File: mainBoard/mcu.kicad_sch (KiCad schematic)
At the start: 20 parts, among them Q1 IRLML6244TRPBF, SW2 SW_SPDT, U4 STM32F401RETx, Y2 ATS08A-E

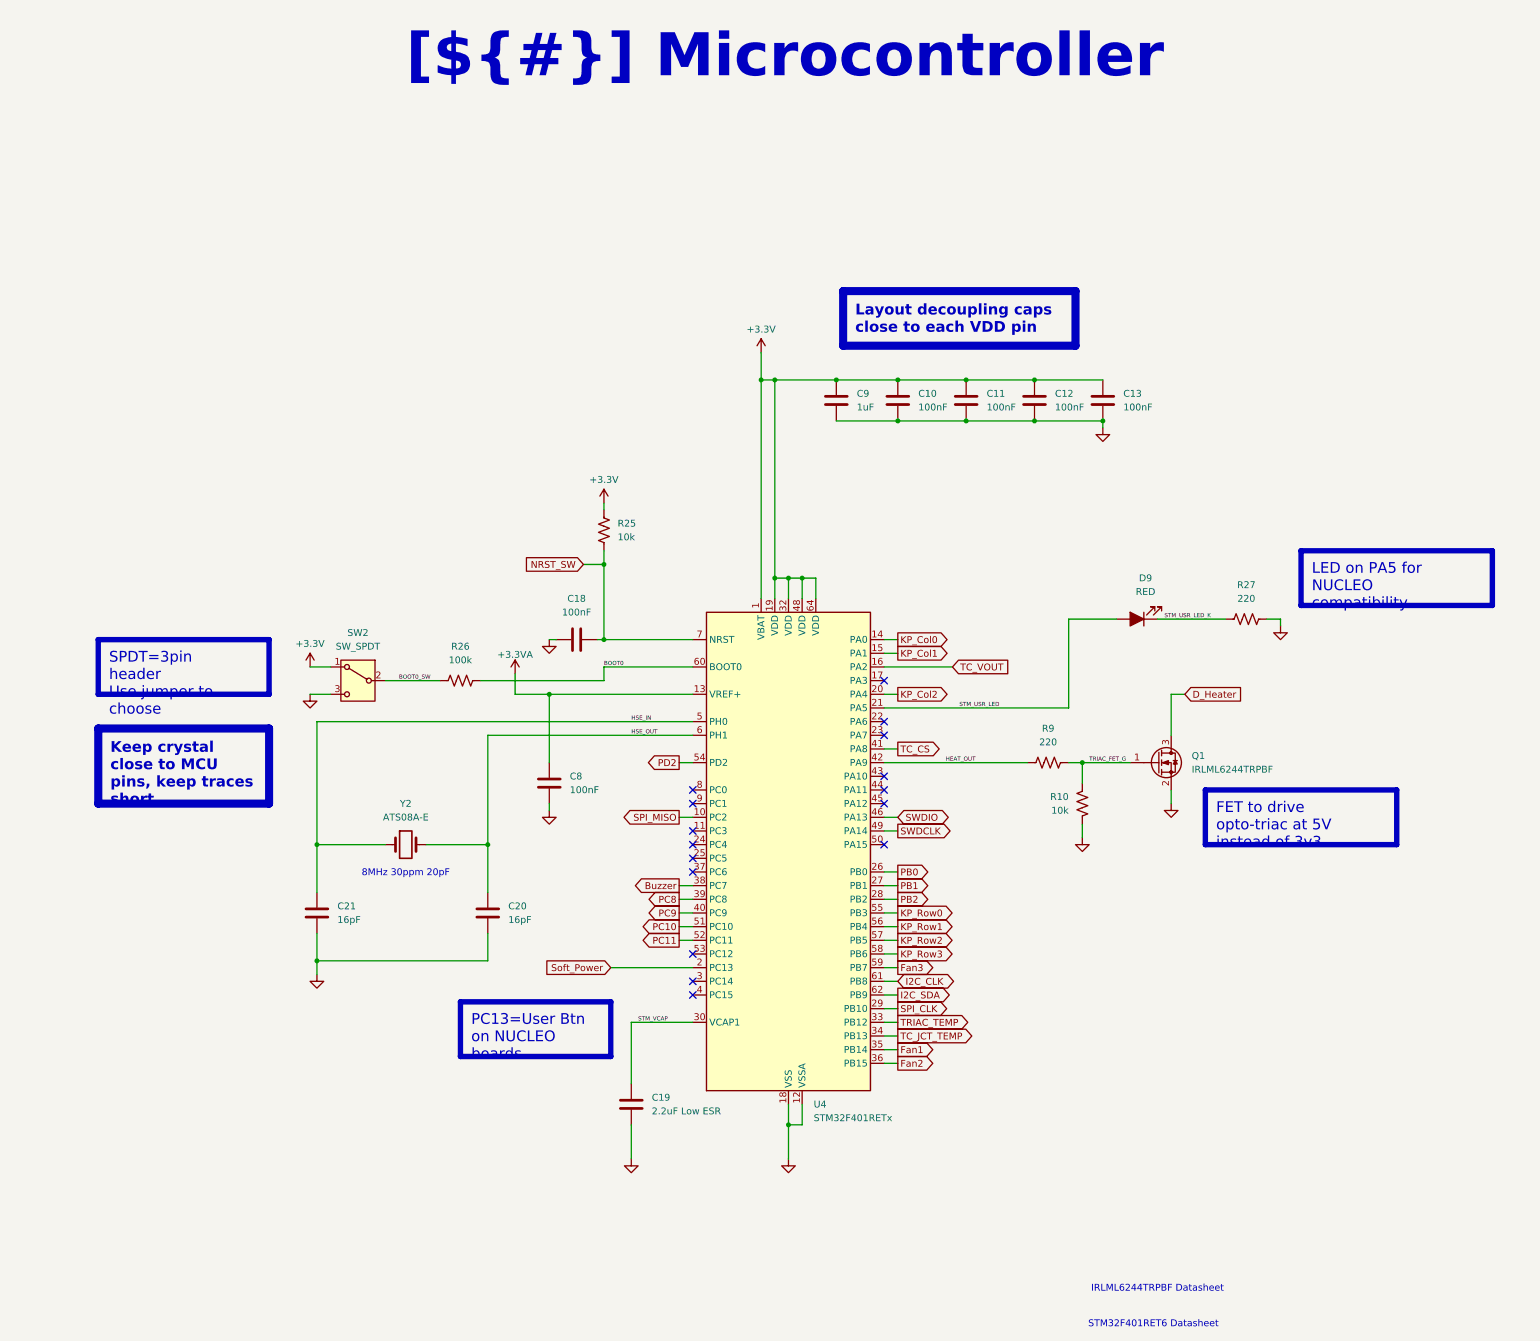
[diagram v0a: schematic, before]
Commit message: Add net colors and tweak MCU
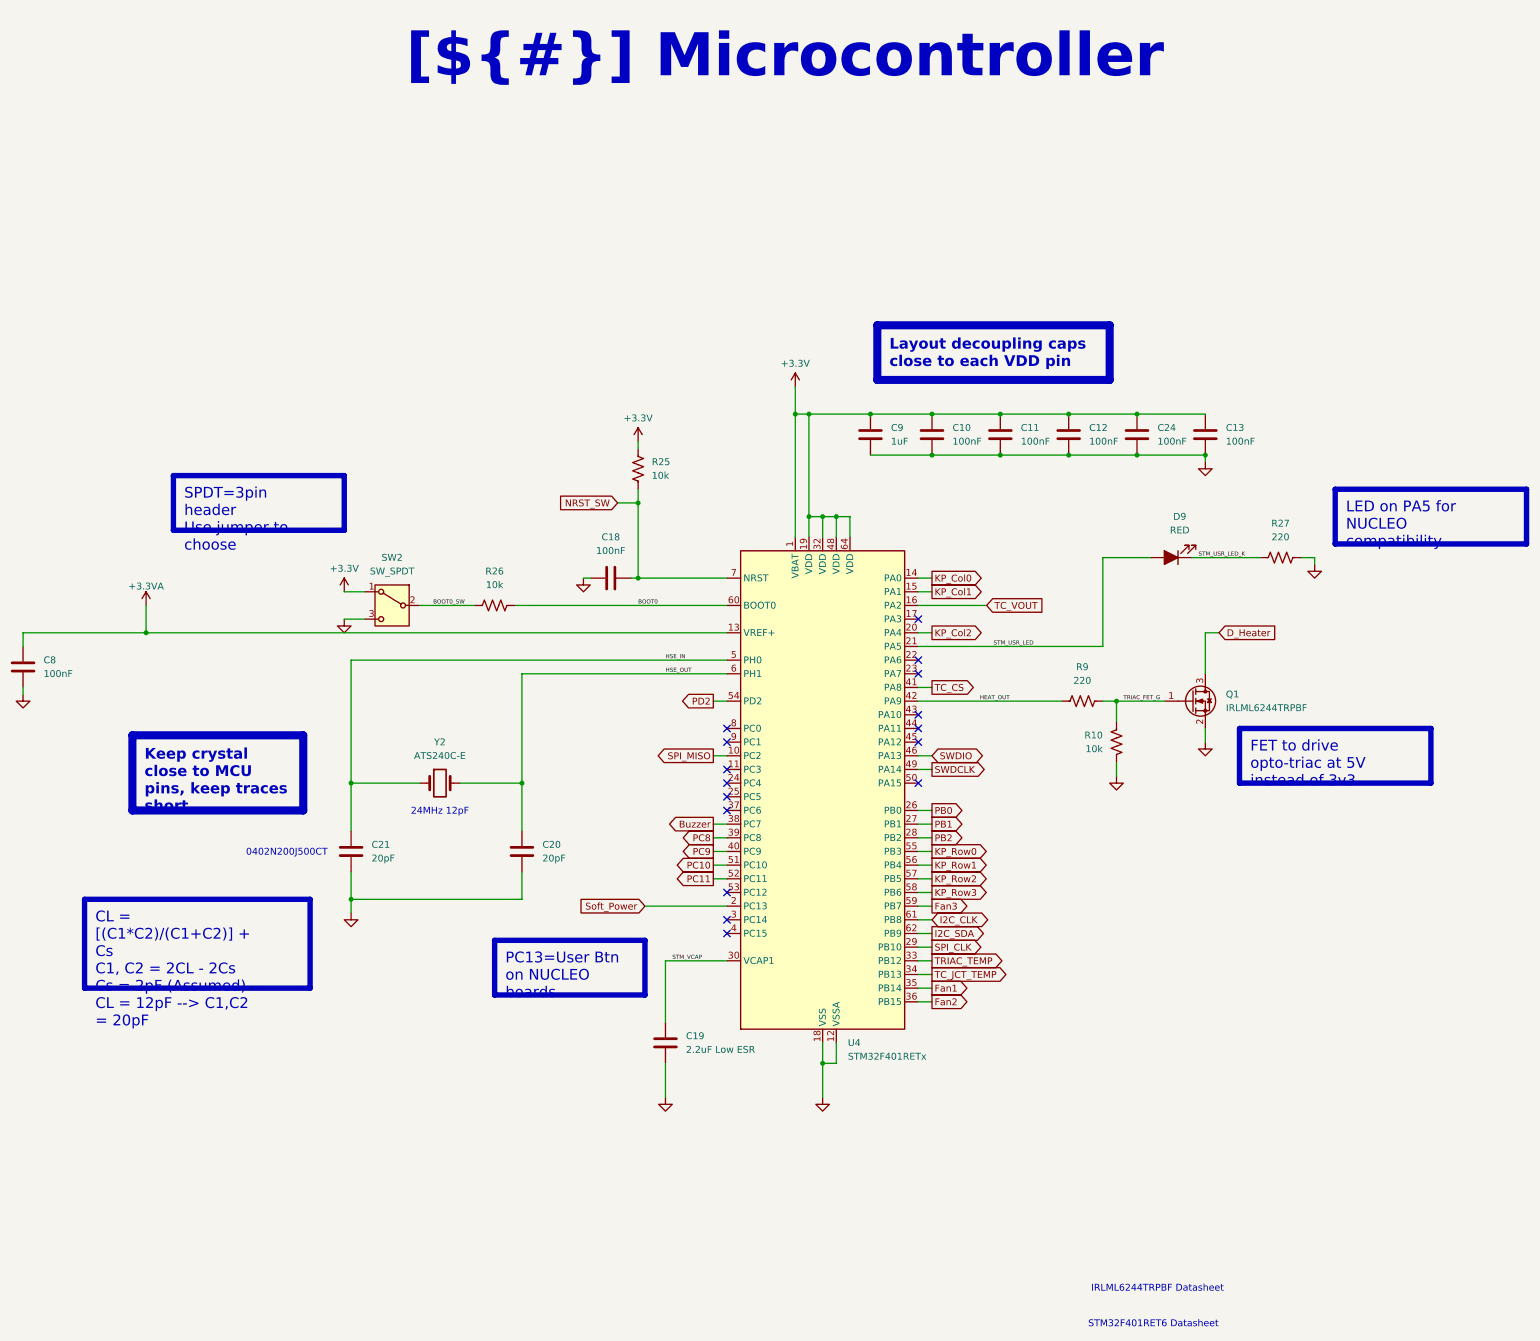
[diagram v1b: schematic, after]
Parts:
- added C24: 100nF, Capacitor_SMD:C_0603_1608Metric_Pad1.08x0.95mm_HandSolder, symbol Device:C
- C20, C21: value 16pF -> 20pF
- R26: value 100k -> 10k
- Y2: value ATS08A-E -> ATS240C-E
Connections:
- net +3.3V: now also C24.1
- net GND: now also C24.2
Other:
- note added: "0402N200J500CT"
- note added: "24MHz 12pF"
- note removed: "8MHz 30ppm 20pF"
- moved on the sheet: C10, C11, C12, C13, C18, C19, C20, C21, C8, C9, D9, Q1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

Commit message: Schematic Capture should be complete, ready for PCB
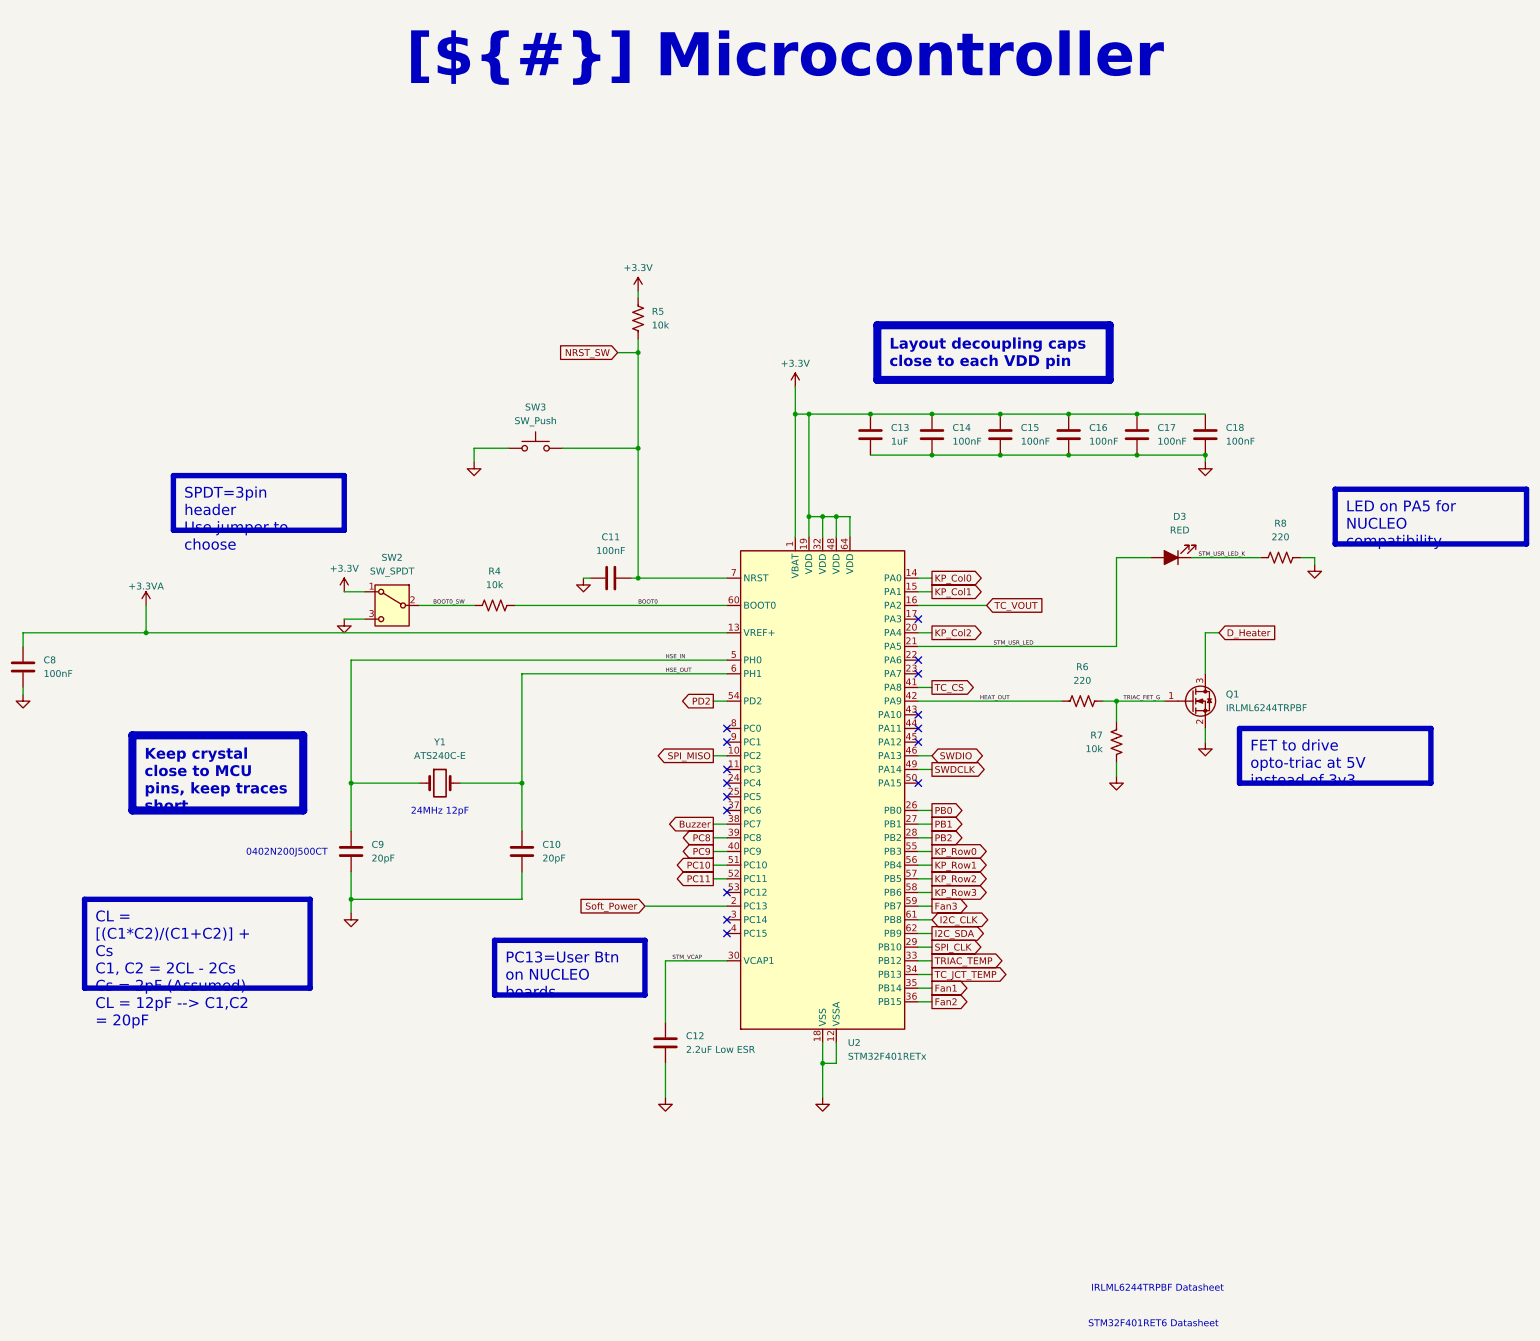
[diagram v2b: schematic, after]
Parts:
- added SW3: SW_Push, Button_Switch_THT:SW_PUSH_6mm_H4.3mm, symbol Switch:SW_Push
- renumbered C20 to C10, C18 to C11, C19 to C12, C9 to C13, C10 to C14, C11 to C15, C12 to C16, C24 to C17, C13 to C18, C21 to C9, D9 to D3, R26 to R4, R25 to R5, R9 to R6, R10 to R7, R27 to R8, U4 to U2, Y2 to Y1
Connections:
- net GND: now also SW3.1
- net NRST_SW: now also SW3.2
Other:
- moved on the sheet: R5

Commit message: tweak schematic for changes from 6-17-2026
major structural changes, see daily note from obsidian
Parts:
- Y1: footprint Crystal:Crystal_HC49-4H_Vertical -> Crystal:Crystal_SMD_3225-4Pin_3.2x2.5mm
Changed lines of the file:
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@@
 			)
 		)
-		(property "Footprint" "Crystal:Crystal_HC49-4H_Vertical"
+		(property "Footprint" "Crystal:Crystal_SMD_3225-4Pin_3.2x2.5mm"
 			(at 146.05 156.21 0)
 			(effects

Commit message: working on pcb layout after bringing in work from laptop
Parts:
- removed Q1: IRLML6244TRPBF, Package_TO_SOT_SMD:SOT-23, symbol Transistor_FET:IRLML6244
- removed R6: 220, Resistor_SMD:R_0603_1608Metric_Pad0.98x0.95mm_HandSolder, symbol Device:R_US
- removed R7: 10k, Resistor_SMD:R_0603_1608Metric_Pad0.98x0.95mm_HandSolder, symbol Device:R_US
- added D14: RED, LED_SMD:LED_0603_1608Metric_Pad1.05x0.95mm_HandSolder, symbol Device:LED_Filled
- added NT3, NT4: NetTie_2, NetTie:NetTie-2_SMD_Pad0.5mm, symbol Device:NetTie_2
- added R58: 220, Resistor_SMD:R_0603_1608Metric_Pad0.98x0.95mm_HandSolder, symbol Device:R_US
- D5: renamed from D3; value RED -> GRN
- renumbered C8 to C14, C9 to C15, C10 to C16, C11 to C17, C12 to C18, C13 to C19, C14 to C20, C15 to C21, C16 to C22, C17 to C23, C18 to C24, R5 to R10, R8 to R11, R4 to R9, U2 to U4
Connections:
- net PC11 is gone; now on net KP_Col0: U4.52 (PC11)
- net PD2 is gone; now on net KP_Col2: U4.54 (PD2)
- net +3.3VA: now also NT4.2; no longer U4.13 (VREF+)
- net Buzzer: now also U4.59 (PB7); no longer U4.38 (PC7)
- net Fan1: now also U4.45 (PA12); no longer U4.35 (PB14)
- net Fan2: now also U4.43 (PA10); no longer U4.36 (PB15)
- net Fan3: now also U4.44 (PA11); no longer U4.59 (PB7)
- net GND: now also NT3.1, R58.2; no longer C15.2, C16.2
- net HSE_IN: now also Y1.2; no longer Y1.1
- net HSE_OUT: now also Y1.1; no longer Y1.2
- net KP_Col0: no longer U4.14 (PA0)
- net KP_Col1: now also U4.53 (PC12); no longer U4.15 (PA1)
- net KP_Col2: no longer U4.20 (PA4)
- net Soft_Power: now also U4.25 (PC5); no longer U4.2 (PC13)
- net TC3_CJ_TEMP: now reaches U4.22 (PA6)
- net TC2_CJ_TEMP: now reaches U4.23 (PA7)
- net TC1_CJ_TEMP: now reaches U4.24 (PC4)
- net STM_USR_LED1: now reaches U4.50 (PA15)
- net STM_USR_LED1: now also D5.2 (A)
- net HEAT_OUT renamed Conv_Fan
- net PC10 renamed STM_USR_LED2
- net STM_USR_LED2: now also D14.2 (A)
- net PC8 renamed TRIAC_BOT_TEMP
- net PC9 renamed Top_Heater
- net SPI_CLK: no longer names the net of U4.29 (PB10)
- net SPI_MISO: no longer names the net of U4.10 (PC2)
- net STM_USR_LED renamed TC1_ADC
- net TC1_ADC: no longer D5.2 (A)
- net STM_USR_LED_K renamed STM_USR_LED1_K
- net TC_CS renamed TRIAC_TOP_TEMP
- net TC_JCT_TEMP: no longer names the net of U4.34 (PB13)
- net TC_VOUT renamed TC3_ADC
- net TRIAC_TEMP: no longer names the net of U4.33 (PB12)
- new net Bottom_Heater: U4.38 (PC7)
- new net HSE_GND: C15.2, C16.2, NT3.2
- new net STM_USR_LED2_K: D14.1 (K), R58.1
- new net STM_VREF: NT4.1, U4.13 (VREF+)
- new net TC2_ADC: U4.20 (PA4)
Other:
- moved on the sheet: C14, D5, R11
